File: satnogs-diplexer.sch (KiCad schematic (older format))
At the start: 13 parts, among them P1 Conn_RF, P2 Conn_RF, P3 Conn_RF

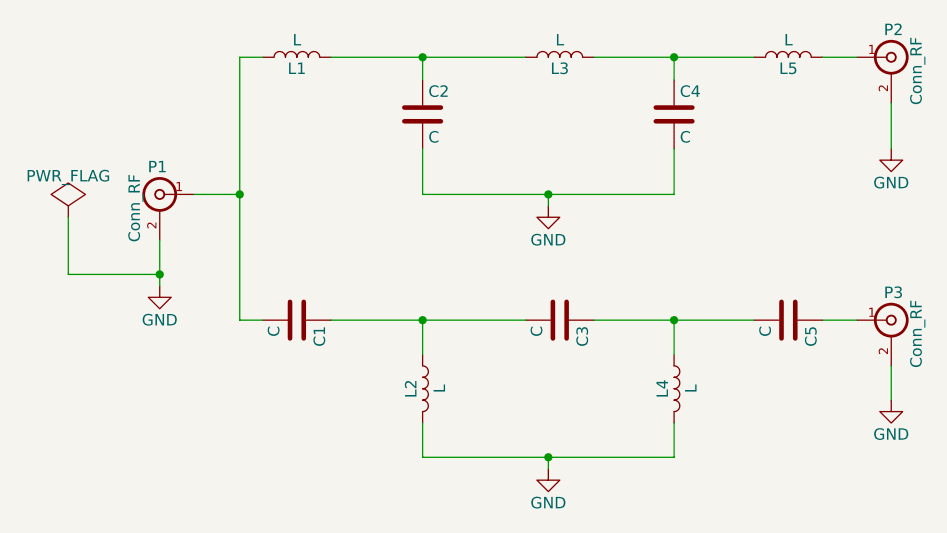
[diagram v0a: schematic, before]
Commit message: Add vias, silksceen to board
Signed-off-by: zisi <agzisim@gmail.com>
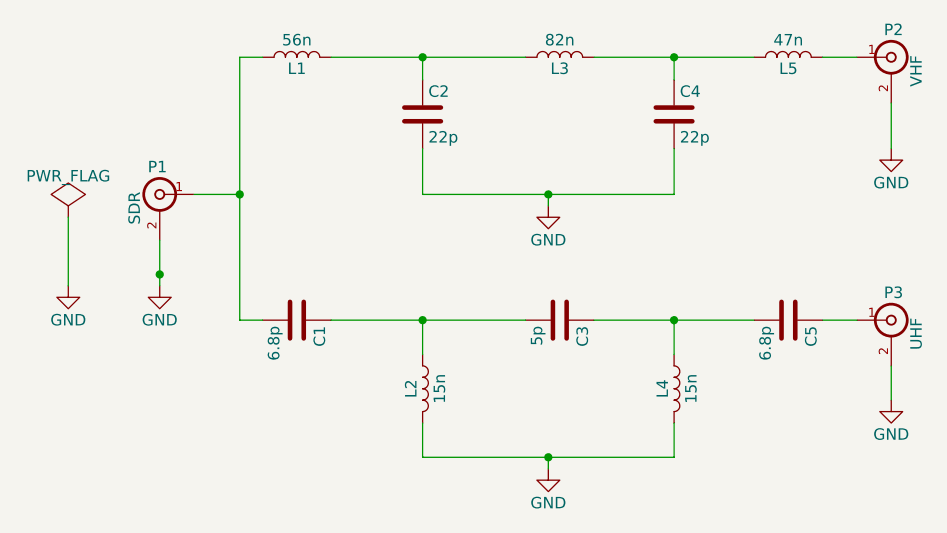
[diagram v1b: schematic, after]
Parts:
- C1, C5: value C -> 6.8p; Mnf. (none) -> GRM1885C1H6R8DA01D
- C2, C4: value C -> 22p; Mnf. (none) -> GRM1885C1H220JA01D
- C3: value C -> 5p; Mnf. (none) -> GQM1885C2A5R0BB01D
- L1: value L -> 56n; Mnf. (none) -> 0603AS056J-YY
- L2, L4: value L -> 15n; Mnf. (none) -> 0603AS-015J-YY
- L3: value L -> 82n; Mnf. (none) -> 0603AS-082J-YY
- L5: value L -> 47n; Mnf. (none) -> 0603AS-047J-YY
- P1: value Conn_RF -> SDR; Mnf. (none) -> 73251-1150
- P2: value Conn_RF -> VHF; Mnf. (none) -> 73251-1150
- P3: value Conn_RF -> UHF; Price 3.13 -> (none)
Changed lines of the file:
@@
 P 4500 3400
 F 0 "C2" H 4525 3500 50  0000 L CNN
-F 1 "C" H 4525 3300 50  0000 L CNN
+F 1 "22p" H 4525 3300 50  0000 L CNN
 F 2 "Capacitors_SMD:C_0603_HandSoldering" H 4538 3250 50  0001 C CNN
 F 3 "" H 4500 3400 50  0000 C CNN
+F 4 "GRM1885C1H220JA01D" H 4500 3400 60  0001 C CNN "Mnf."
 	1    4500 3400
 	1    0    0    -1
@@
 P 5600 3400
 F 0 "C4" H 5625 3500 50  0000 L CNN
-F 1 "C" H 5625 3300 50  0000 L CNN
+F 1 "22p" H 5625 3300 50  0000 L CNN
 F 2 "Capacitors_SMD:C_0603_HandSoldering" H 5638 3250 50  0001 C CNN
 F 3 "" H 5600 3400 50  0000 C CNN
+F 4 "GRM1885C1H220JA01D" H 5600 3400 60  0001 C CNN "Mnf."
 	1    5600 3400
 	1    0    0    -1
@@
 P 3950 4300
 F 0 "C1" H 3975 4400 50  0000 L CNN
-F 1 "C" H 3975 4200 50  0000 L CNN
+F 1 "6.8p" H 3975 4200 50  0000 L CNN
 F 2 "Capacitors_SMD:C_0603_HandSoldering" H 3988 4150 50  0001 C CNN
 F 3 "" H 3950 4300 50  0000 C CNN
+F 4 "GRM1885C1H6R8DA01D" H 3950 4300 60  0001 C CNN "Mnf."
 	1    3950 4300
 	0    1    1    0
@@
 P 5100 4300
 F 0 "C3" H 5125 4400 50  0000 L CNN
-F 1 "C" H 5125 4200 50  0000 L CNN
+F 1 "5p" H 5125 4200 50  0000 L CNN
 F 2 "Capacitors_SMD:C_0603_HandSoldering" H 5138 4150 50  0001 C CNN
 F 3 "" H 5100 4300 50  0000 C CNN
+F 4 "GQM1885C2A5R0BB01D" H 5100 4300 60  0001 C CNN "Mnf."
 	1    5100 4300
 	0    1    1    0
@@
 P 6100 4300
 F 0 "C5" H 6125 4400 50  0000 L CNN
-F 1 "C" H 6125 4200 50  0000 L CNN
+F 1 "6.8p" H 6125 4200 50  0000 L CNN
 F 2 "Capacitors_SMD:C_0603_HandSoldering" H 6138 4150 50  0001 C CNN
 F 3 "" H 6100 4300 50  0000 C CNN
+F 4 "GRM1885C1H6R8DA01D" H 6100 4300 60  0001 C CNN "Mnf."
 	1    6100 4300
 	0    1    1    0
@@
 P 4500 4600
 F 0 "L2" V 4450 4600 50  0000 C CNN
-F 1 "L" V 4575 4600 50  0000 C CNN
+F 1 "15n" V 4575 4600 50  0000 C CNN
 F 2 "Resistors_SMD:R_0603_HandSoldering" H 4500 4600 50  0001 C CNN
 F 3 "" H 4500 4600 50  0000 C CNN
+F 4 "0603AS-015J-YY" V 4500 4600 60  0001 C CNN "Mnf."
 	1    4500 4600
 	1    0    0    -1
@@
 P 5600 4600
 F 0 "L4" V 5550 4600 50  0000 C CNN
-F 1 "L" V 5675 4600 50  0000 C CNN
+F 1 "15n" V 5675 4600 50  0000 C CNN
 F 2 "Resistors_SMD:R_0603_HandSoldering" H 5600 4600 50  0001 C CNN
 F 3 "" H 5600 4600 50  0000 C CNN
+F 4 "0603AS-015J-YY" V 5600 4600 60  0001 C CNN "Mnf."
 	1    5600 4600
 	1    0    0    -1
@@
 P 3950 3150
 F 0 "L1" V 3900 3150 50  0000 C CNN
-F 1 "L" V 4025 3150 50  0000 C CNN
+F 1 "56n" V 4025 3150 50  0000 C CNN
 F 2 "Resistors_SMD:R_0603_HandSoldering" H 3950 3150 50  0001 C CNN
 F 3 "" H 3950 3150 50  0000 C CNN
+F 4 "0603AS056J-YY" V 3950 3150 60  0001 C CNN "Mnf."
 	1    3950 3150
 	0    -1   -1   0
@@
 P 5100 3150
 F 0 "L3" V 5050 3150 50  0000 C CNN
-F 1 "L" V 5175 3150 50  0000 C CNN
+F 1 "82n" V 5175 3150 50  0000 C CNN
 F 2 "Resistors_SMD:R_0603_HandSoldering" H 5100 3150 50  0001 C CNN
 F 3 "" H 5100 3150 50  0000 C CNN
+F 4 "0603AS-082J-YY" V 5100 3150 60  0001 C CNN "Mnf."
 	1    5100 3150
 	0    -1   -1   0
@@
 P 6100 3150
 F 0 "L5" V 6050 3150 50  0000 C CNN
-F 1 "L" V 6175 3150 50  0000 C CNN
+F 1 "47n" V 6175 3150 50  0000 C CNN
 F 2 "Resistors_SMD:R_0603_HandSoldering" H 6100 3150 50  0001 C CNN
 F 3 "" H 6100 3150 50  0000 C CNN
+F 4 "0603AS-047J-YY" V 6100 3150 60  0001 C CNN "Mnf."
 	1    6100 3150
 	0    -1   -1   0
@@
 	6250 3150 6400 3150
 $Comp
-L GND #PWR01
+L GND #PWR3
 U 1 1 58A74AED
 P 5050 3800
-F 0 "#PWR01" H 5050 3550 50  0001 C CNN
+F 0 "#PWR3" H 5050 3550 50  0001 C CNN
 F 1 "GND" H 5050 3650 50  0000 C CNN
 F 2 "" H 5050 3800 50  0000 C CNN
@@
 $EndComp
 $Comp
-L GND #PWR02
+L GND #PWR4
 U 1 1 58A74B6F
 P 5050 4950
-F 0 "#PWR02" H 5050 4700 50  0001 C CNN
+F 0 "#PWR4" H 5050 4700 50  0001 C CNN
 F 1 "GND" H 5050 4800 50  0000 C CNN
 F 2 "" H 5050 4950 50  0000 C CNN
@@
 	3350 3950 3350 4150
 $Comp
-L GND #PWR03
+L GND #PWR2
 U 1 1 58A7567A
 P 3350 4150
-F 0 "#PWR03" H 3350 3900 50  0001 C CNN
+F 0 "#PWR2" H 3350 3900 50  0001 C CNN
 F 1 "GND" H 3350 4000 50  0000 C CNN
 F 2 "" H 3350 4150 50  0000 C CNN
@@
 $EndComp
 $Comp
-L GND #PWR04
+L GND #PWR6
 U 1 1 58A7572E
 P 6550 4650
-F 0 "#PWR04" H 6550 4400 50  0001 C CNN
+F 0 "#PWR6" H 6550 4400 50  0001 C CNN
 F 1 "GND" H 6550 4500 50  0000 C CNN
 F 2 "" H 6550 4650 50  0000 C CNN
@@
 $EndComp
 $Comp
-L GND #PWR05
+L GND #PWR5
 U 1 1 58A757AE
 P 6550 3550
-F 0 "#PWR05" H 6550 3300 50  0001 C CNN
+F 0 "#PWR5" H 6550 3300 50  0001 C CNN
 F 1 "GND" H 6550 3400 50  0000 C CNN
 F 2 "" H 6550 3550 50  0000 C CNN
@@
 $EndComp
 $Comp
-L PWR_FLAG #FLG06
+L PWR_FLAG #FLG1
 U 1 1 58A75A83
 P 2950 3850
-F 0 "#FLG06" H 2950 3945 50  0001 C CNN
+F 0 "#FLG1" H 2950 3945 50  0001 C CNN
 F 1 "PWR_FLAG" H 2950 4030 50  0000 C CNN
 F 2 "" H 2950 3850 50  0000 C CNN
@@
 $EndComp
 Wire Wire Line
-	2950 3850 2950 4100
-Wire Wire Line
-	2950 4100 3350 4100
+	2950 3850 2950 4150
 Connection ~ 3350 4100
 $Comp
@@
 P 6550 3150
 F 0 "P2" H 6560 3270 50  0000 C CNN
-F 1 "Conn_RF" V 6660 3090 50  0000 C CNN
+F 1 "VHF" V 6660 3090 50  0000 C CNN
 F 2 "Conn_RF:Conn_SMA_Molex_73251-1150" H 6550 3150 50  0001 C CNN
 F 3 "" H 6550 3150 50  0000 C CNN
+F 4 "73251-1150" H 6550 3150 60  0001 C CNN "Mnf."
 	1    6550 3150
 	1    0    0    -1
@@
 P 6550 4300
 F 0 "P3" H 6560 4420 50  0000 C CNN
-F 1 "Conn_RF" V 6660 4240 50  0000 C CNN
+F 1 "UHF" V 6660 4240 50  0000 C CNN
 F 2 "Conn_RF:Conn_SMA_Molex_73251-1150" H 6550 4300 50  0001 C CNN
 F 3 "" H 6550 4300 50  0000 C CNN
 F 4 "73251-1150" H 6550 4300 60  0001 C CNN "Mnf."
-F 5 "3.13" H 6550 4300 60  0001 C CNN "Price"
 	1    6550 4300
 	1    0    0    -1
@@
 P 3350 3750
 F 0 "P1" H 3360 3870 50  0000 C CNN
-F 1 "Conn_RF" V 3460 3690 50  0000 C CNN
+F 1 "SDR" V 3460 3690 50  0000 C CNN
 F 2 "Conn_RF:Conn_SMA_Molex_73251-1150" H 3350 3750 50  0001 C CNN
 F 3 "" H 3350 3750 50  0000 C CNN
+F 4 "73251-1150" H 3350 3750 60  0001 C CNN "Mnf."
 	1    3350 3750
 	-1   0    0    -1
 $EndComp
+$Comp
+L GND #PWR1
+U 1 1 58B45B85
+P 2950 4150
+F 0 "#PWR1" H 2950 3900 50  0001 C CNN
+F 1 "GND" H 2950 4000 50  0000 C CNN
+F 2 "" H 2950 4150 50  0000 C CNN
+F 3 "" H 2950 4150 50  0000 C CNN
+	1    2950 4150
+	1    0    0    -1
+$EndComp
 $EndSCHEMATC

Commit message: FIxes #3
Signed-off-by: Agis Zisimatos <agzisim@gmail.com>
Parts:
- C1, C2, C3, C4, C5: footprint Capacitors_SMD:C_0603_HandSoldering -> Capacitor_SMD:C_0603_1608Metric; symbol C -> Device:C
- L1, L2, L3, L4, L5: footprint Resistors_SMD:R_0603_HandSoldering -> Inductor_SMD:L_0603_1608Metric; symbol L -> Device:L
- P1, P2, P3: footprint Conn_RF:Conn_SMA_Molex_73251-1150 -> Connector_Coaxial:SMA_Amphenol_132289_EdgeMount; symbol Conn_RF -> Connector:Conn_Coaxial; Mnf. 73251-1150 -> 132289
